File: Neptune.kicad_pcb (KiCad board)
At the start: 4 copper layers, 191.2 x 190.9 mm, 379 parts, among them CN2 Expansion, CN3 Cartridge, CN5 1P, CN504 AV Out, CN6 2P, CN7 Barrel_Jack, IC1 68HC000, IC2 LHP6323, IC4 Z80CPU, IC5 LC3664, IC501 SH2 M, IC502 SH2 S, IC503 µPD4502161, IC504 315-5818, IC505 315-5805, IC506 315-5781, IC507 TC511664, IC508 TC511664, IC509 74AC04, IC510 RHSRL33A, IC511 315-5684, IC512 315-5788, IC515 74HC74, IC516 74LS00, IC6 315-5660, IC601 74ACT241, IC7 MSM54C864, IC701 PIC16F630/18324, IC801 TPS564257DRLR, IC901 TL972, IC951 THS7374, J2 EXT, Q801 MMBT3904, X501 *3

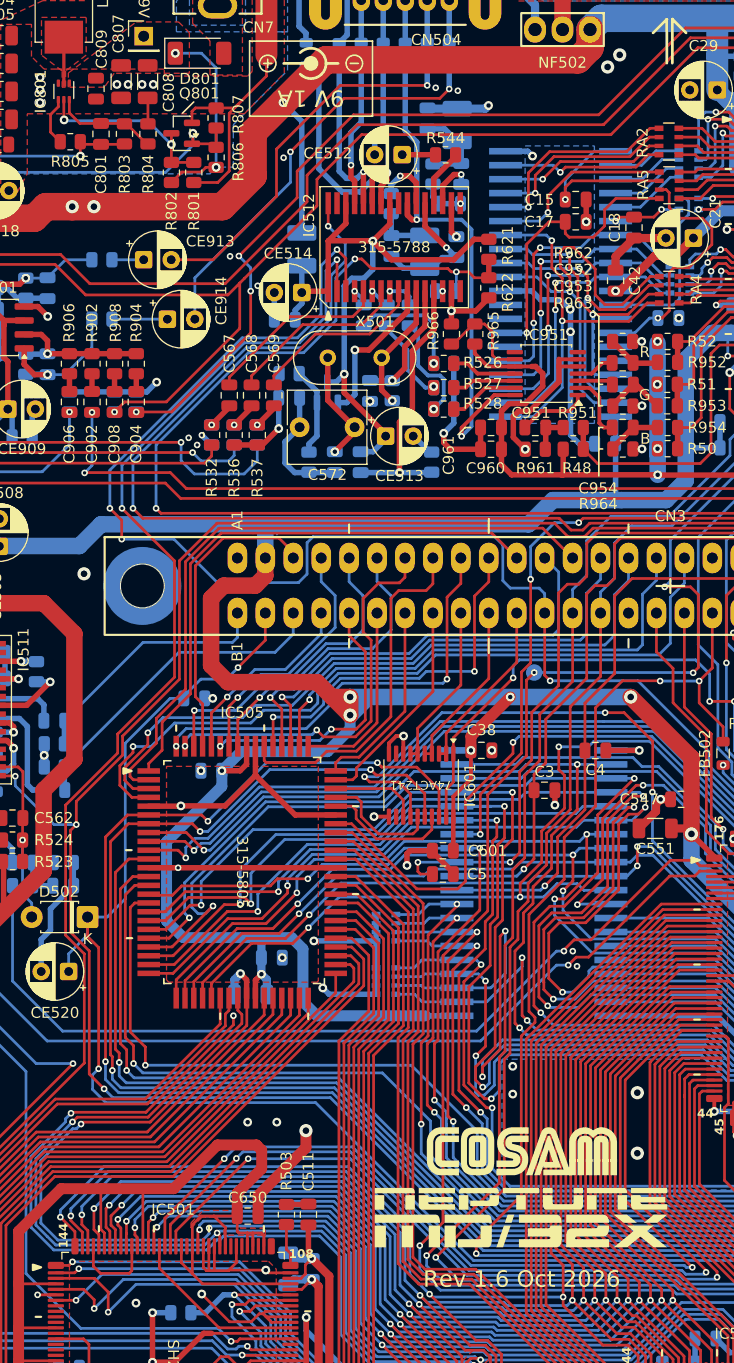
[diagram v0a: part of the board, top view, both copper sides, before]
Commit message: Clearer pin 1 indicator for IC801.
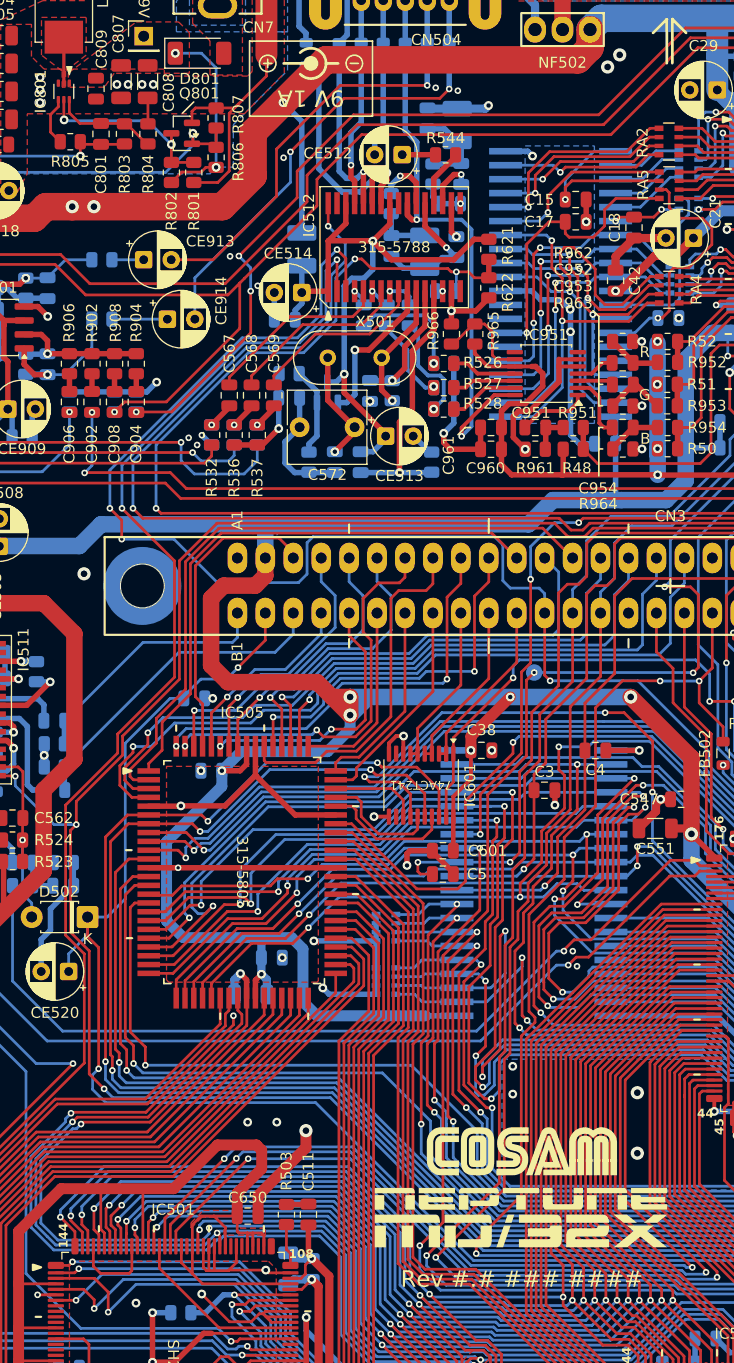
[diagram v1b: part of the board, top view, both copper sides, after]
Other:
- board text added: "Rev #.# ### ####"
- board text removed: "Rev 1.6 Oct 2026"
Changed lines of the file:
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@@
 		)
 		(fp_line
-			(start -0.9 -0.9)
+			(start -0.65 -0.9)
 			(end 0.65 -0.9)
 			(stroke
@@
 			(layer "F.SilkS")
 		)
+		(fp_poly
+			(pts
+				(xy -1.5 -0.5) (xy -2.262 -0.754) (xy -2.262 -0.246)
+			)
+			(stroke
+				(width 0.1)
+				(type solid)
+			)
+			(fill yes)
+			(layer "F.SilkS")
+		)
 		(fp_line
 			(start 1.35 1.1)
@@
 		)
 	)
-	(gr_text "Rev 1.6 Oct 2026"
+	(gr_text "Rev #.# ### ####"
 		(at 193.4 170.575 0)
 		(layer "F.SilkS")
